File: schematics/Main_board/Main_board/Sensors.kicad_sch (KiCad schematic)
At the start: 13 parts, among them J3 Conn_01x06_Female, J4 Conn_01x06_Female, J5 Conn_01x06_Female, U5 PCF8563T, U6 LCD, U7 LSM6DS3, Y2 32.768kHz

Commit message: fix: 3d step file paths
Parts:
- C10, C11, C8: footprint Capacitor_SMD:C_0201_0603Metric -> Capacitor_SMD:C_0402_1005Metric
- R4, R5: footprint Resistor_SMD:R_0603_1608Metric_Pad0.98x0.95mm_HandSolder -> Resistor_SMD:R_0402_1005Metric
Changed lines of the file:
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@@
       (effects (font (size 1.27 1.27)))
     )
-    (property "Footprint" "Capacitor_SMD:C_0201_0603Metric" (at 30.48 36.5252 0)
+    (property "Footprint" "Capacitor_SMD:C_0402_1005Metric" (at 30.48 36.5252 0)
       (effects (font (size 1.27 1.27)) hide)
     )
@@
       (effects (font (size 1.27 1.27)))
     )
-    (property "Footprint" "Capacitor_SMD:C_0201_0603Metric" (at 80.01 88.5952 0)
+    (property "Footprint" "Capacitor_SMD:C_0402_1005Metric" (at 80.01 88.5952 0)
       (effects (font (size 1.27 1.27)) hide)
     )
@@
       (effects (font (size 1.27 1.27)) (justify left))
     )
-    (property "Footprint" "Resistor_SMD:R_0603_1608Metric_Pad0.98x0.95mm_HandSolder" (at 33.782 154.94 90)
+    (property "Footprint" "Resistor_SMD:R_0402_1005Metric" (at 33.782 154.94 90)
       (effects (font (size 1.27 1.27)) hide)
     )
@@
       (effects (font (size 1.27 1.27)))
     )
-    (property "Footprint" "Capacitor_SMD:C_0201_0603Metric" (at 69.85 88.5952 0)
+    (property "Footprint" "Capacitor_SMD:C_0402_1005Metric" (at 69.85 88.5952 0)
       (effects (font (size 1.27 1.27)) hide)
     )
@@
       (effects (font (size 1.27 1.27)) (justify right))
     )
-    (property "Footprint" "Resistor_SMD:R_0603_1608Metric_Pad0.98x0.95mm_HandSolder" (at 29.718 154.94 90)
-      (effects (font (size 1.27 1.27)) hide)
-    )
+    (property "Footprint" "Resistor_SMD:R_0402_1005Metric" (at 29.718 154.94 90)
+      (effects (font (size 1.27 1.27)) hide)
+    )

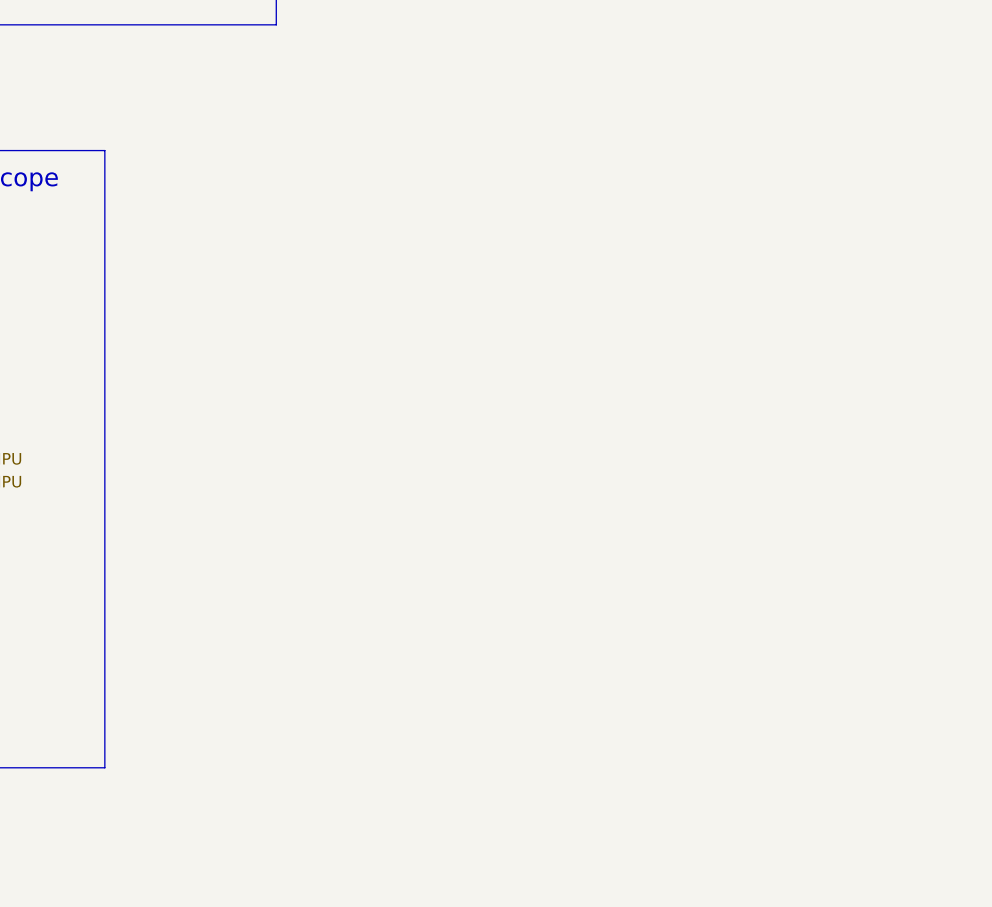
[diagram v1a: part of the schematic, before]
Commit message: update: All the resistors and capacitors footprints changed from 0603 to 0402
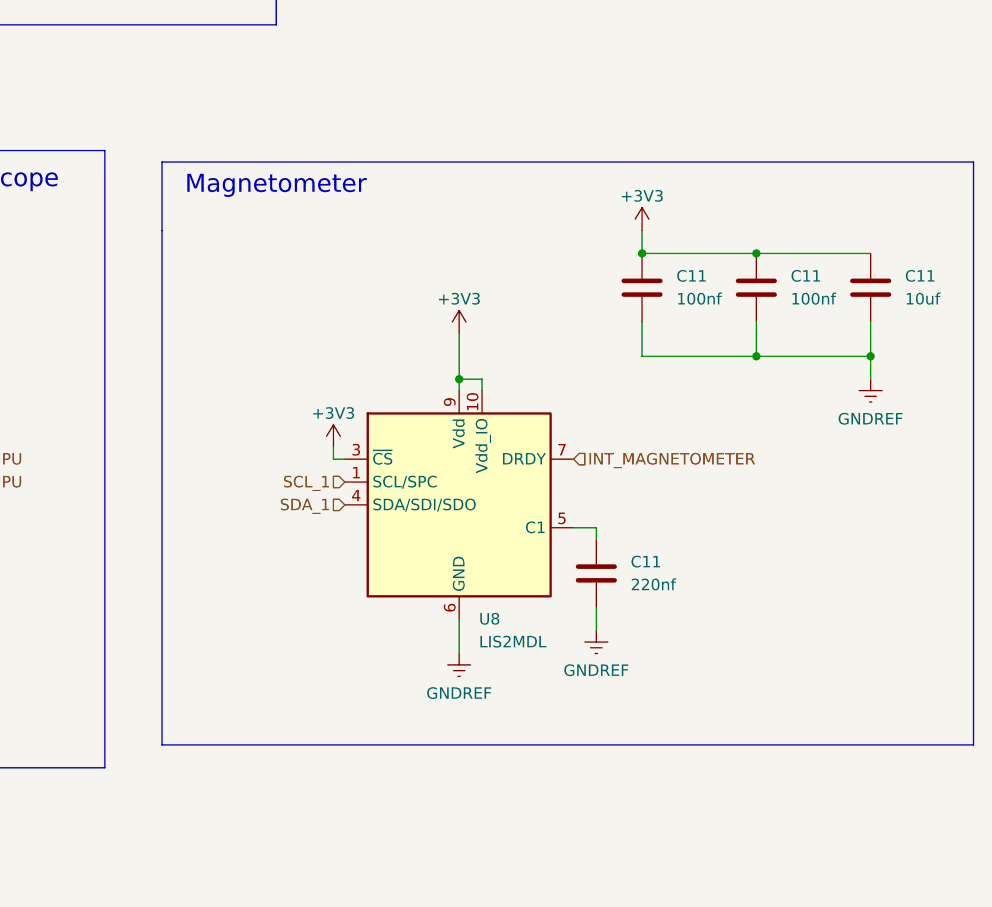
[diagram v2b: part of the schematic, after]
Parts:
- added C11: 220nf, Capacitor_SMD:C_0402_1005Metric, symbol Device:C
- added C11 (x2): 100nf, Capacitor_SMD:C_0402_1005Metric, symbol Device:C
- added C11: 10uf, Capacitor_SMD:C_0402_1005Metric, symbol Device:C
- added U8: LIS2MDL, Package_LGA:LGA-12_2x2mm_P0.5mm, symbol Sensor_Magnetic:LIS2MDL
- Y2: footprint Crystal:Crystal_C38-LF_D3.0mm_L8.0mm_Horizontal -> Crystal:Crystal_SMD_3215-2Pin_3.2x1.5mm; #LCSC Part (none) -> C97606
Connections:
- net +3V3: now also C11.1, C11.1, C11.1, U8.10 (Vdd_IO), U8.3 (~{CS}), U8.9 (Vdd)
- net GNDREF: now also C11.2, C11.2, C11.2, C11.2, U8.6 (GND), U8.8 (GND)
- net SCL_1: now also U8.1 (SCL/SPC)
- net SDA_1: now also U8.4 (SDA/SDI/SDO)
- new net: C11.1, U8.5 (C1)
- new net INT_MAGNETOMETER: U8.7 (DRDY)
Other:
- note added: "Magnetometer"
